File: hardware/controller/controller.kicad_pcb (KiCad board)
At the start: 4 copper layers, 59 x 47 mm, 62 parts, among them J1 Conn_01x02_Pin, J11 Barrel_Jack, J12 USB_C_Receptacle_USB2.0_14P, J2 Conn_01x02_Pin, J3 Conn_01x02_Pin, J5 Screw_Terminal_01x02, J6 Screw_Terminal_01x02, J7 Conn_01x04_Pin, J8 Conn_01x04_Pin, U1 ESP32-C3-MINI-1, U2 MAX31855KASA, U3 MAX31855KASA, U4 MAX31855KASA, U5 TPS2121RUXR, U6 TPS1H200AQDGNRQ1, U7 LP2985-3.3, U8 AP63203WU

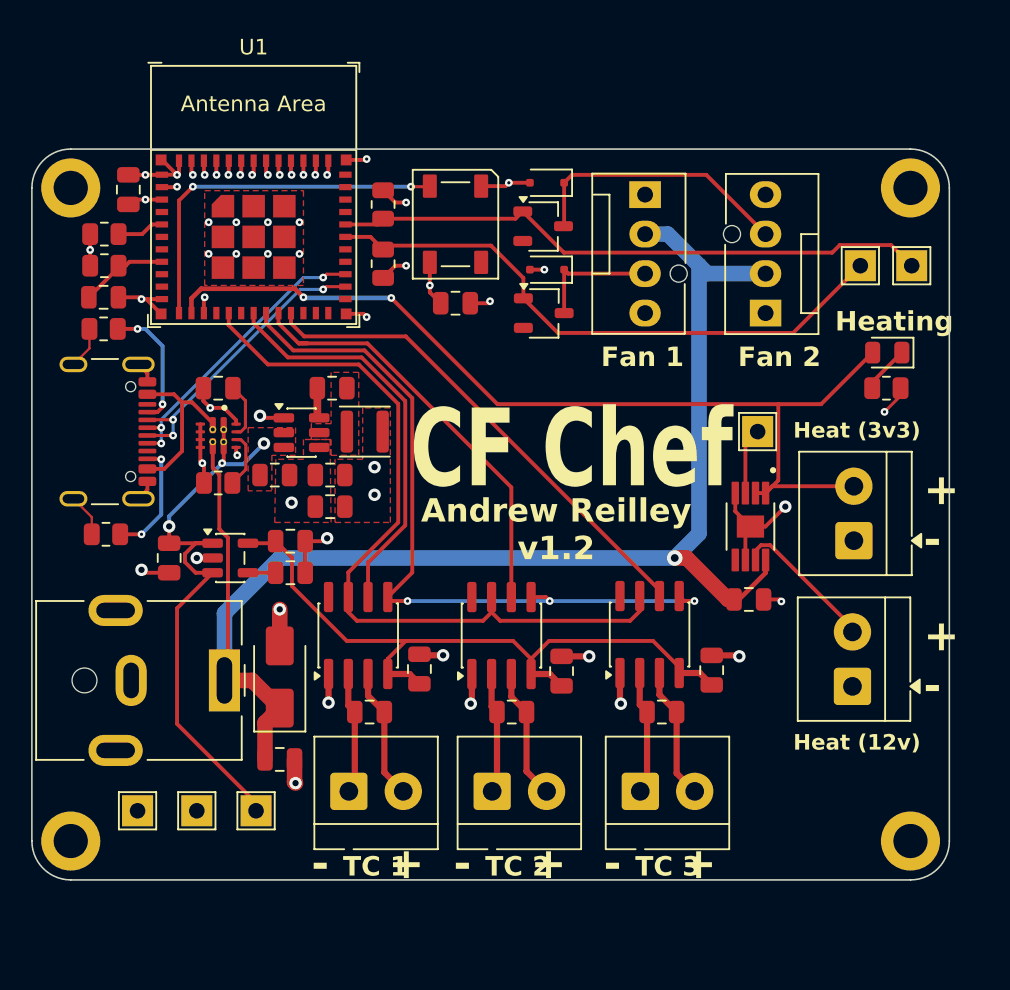
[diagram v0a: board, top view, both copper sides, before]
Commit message: Add ferrites and more caps to thermocouples
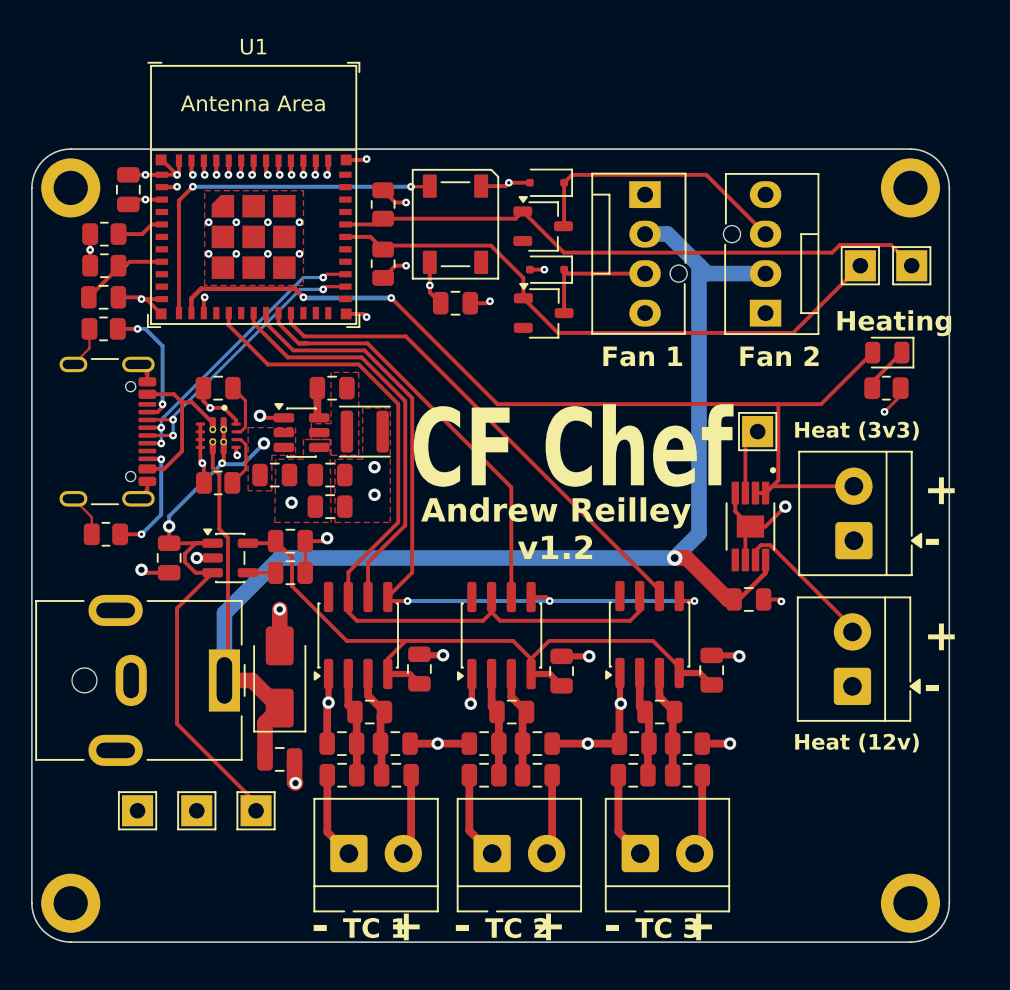
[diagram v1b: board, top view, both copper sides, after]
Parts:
- added C20: 10nF, Capacitor_SMD:C_0805_2012Metric, F.Cu at (146.0, 110.2)
- added C21: 10nF, Capacitor_SMD:C_0805_2012Metric, F.Cu at (149.4, 110.2)
- added C22: 10nF, Capacitor_SMD:C_0805_2012Metric, F.Cu at (127.2, 110.2)
- added C23: 10nF, Capacitor_SMD:C_0805_2012Metric, F.Cu at (130.6, 110.2)
- added C24: 10nF, Capacitor_SMD:C_0805_2012Metric, F.Cu at (136.3, 110.2)
- added C25: 10nF, Capacitor_SMD:C_0805_2012Metric, F.Cu at (139.8, 110.2)
- added FB1: FerriteBead_Small, Capacitor_SMD:C_0805_2012Metric, F.Cu at (130.7, 112.3)
- added FB2: FerriteBead_Small, Capacitor_SMD:C_0805_2012Metric, F.Cu at (127.2, 112.3)
- added FB3: FerriteBead_Small, Capacitor_SMD:C_0805_2012Metric, F.Cu at (139.8, 112.3)
- added FB4: FerriteBead_Small, Capacitor_SMD:C_0805_2012Metric, F.Cu at (136.3, 112.3)
- added FB5: FerriteBead_Small, Capacitor_SMD:C_0805_2012Metric, F.Cu at (149.4, 112.3)
- added FB6: FerriteBead_Small, Capacitor_SMD:C_0805_2012Metric, F.Cu at (145.9, 112.3)
- moved H3 4.00 mm to (109.8, 120.5)
- moved H4 4.00 mm to (163.8, 120.5)
- moved J1 4.00 mm to (127.6, 117.3)
- moved J2 4.00 mm to (136.8, 117.3)
- moved J3 4.00 mm to (146.4, 117.3)
- moved C15 0.13 mm to (147.6, 108.2)
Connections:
- C14 pad 1: Net-(J1-Pin_2) -> Net-(U2-T+)
- C14 pad 2: Net-(J1-Pin_1) -> Net-(U2-T-)
- C15 pad 1: Net-(J3-Pin_2) -> Net-(U4-T+)
- C15 pad 2: Net-(J3-Pin_1) -> Net-(U4-T-)
- C16 pad 1: Net-(J2-Pin_2) -> Net-(U3-T+)
- C16 pad 2: Net-(J2-Pin_1) -> Net-(U3-T-)
- U2 pad 2: Net-(J1-Pin_1) -> Net-(U2-T-)
- U2 pad 3: Net-(J1-Pin_2) -> Net-(U2-T+)
- U3 pad 2: Net-(J2-Pin_1) -> Net-(U3-T-)
- U3 pad 3: Net-(J2-Pin_2) -> Net-(U3-T+)
- U4 pad 2: Net-(J3-Pin_1) -> Net-(U4-T-)
- U4 pad 3: Net-(J3-Pin_2) -> Net-(U4-T+)
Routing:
- net GND: track 79.6 -> 94.8 mm, vias 48 -> 51
- net Net-(U2-T+): track 0.00 -> 7.08 mm
- net Net-(U4-T+): track 0.00 -> 7.02 mm
- net Net-(U3-T+): track 0.00 -> 7.02 mm
- net Net-(U4-T-): track 0.00 -> 6.85 mm
- net Net-(U2-T-): track 0.00 -> 6.74 mm
- net Net-(U3-T-): track 0.00 -> 6.70 mm
- net Net-(J3-Pin_2): track 8.55 -> 5.24 mm
- net Net-(J2-Pin_2): track 8.48 -> 5.18 mm
- net Net-(J1-Pin_2): track 8.49 -> 5.25 mm
- net Net-(J1-Pin_1): track 8.83 -> 5.61 mm
- net Net-(J2-Pin_1): track 8.77 -> 5.65 mm
- net Net-(J3-Pin_1): track 8.68 -> 5.62 mm
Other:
- board size 59 x 47 mm -> 59 x 51 mm
